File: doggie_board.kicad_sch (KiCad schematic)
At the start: 0 parts

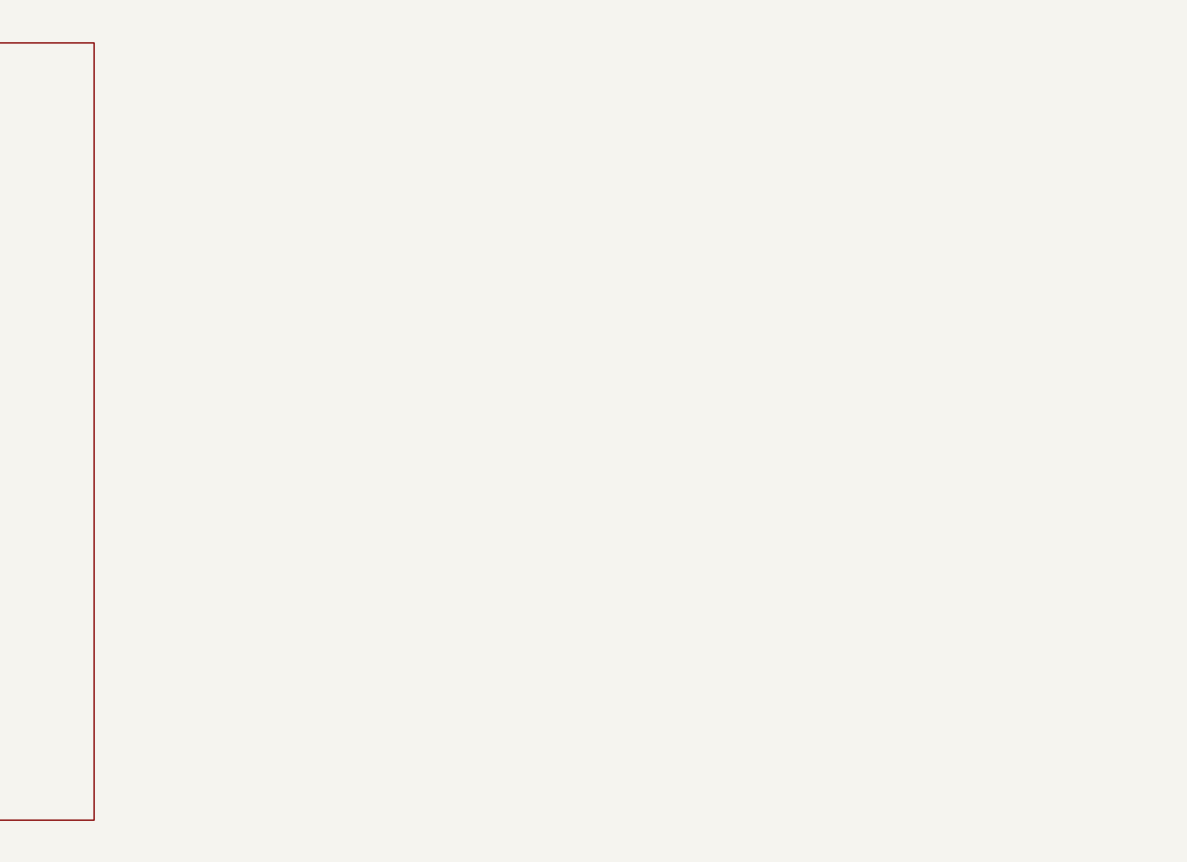
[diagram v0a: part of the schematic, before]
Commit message: Addition of Buck Converter
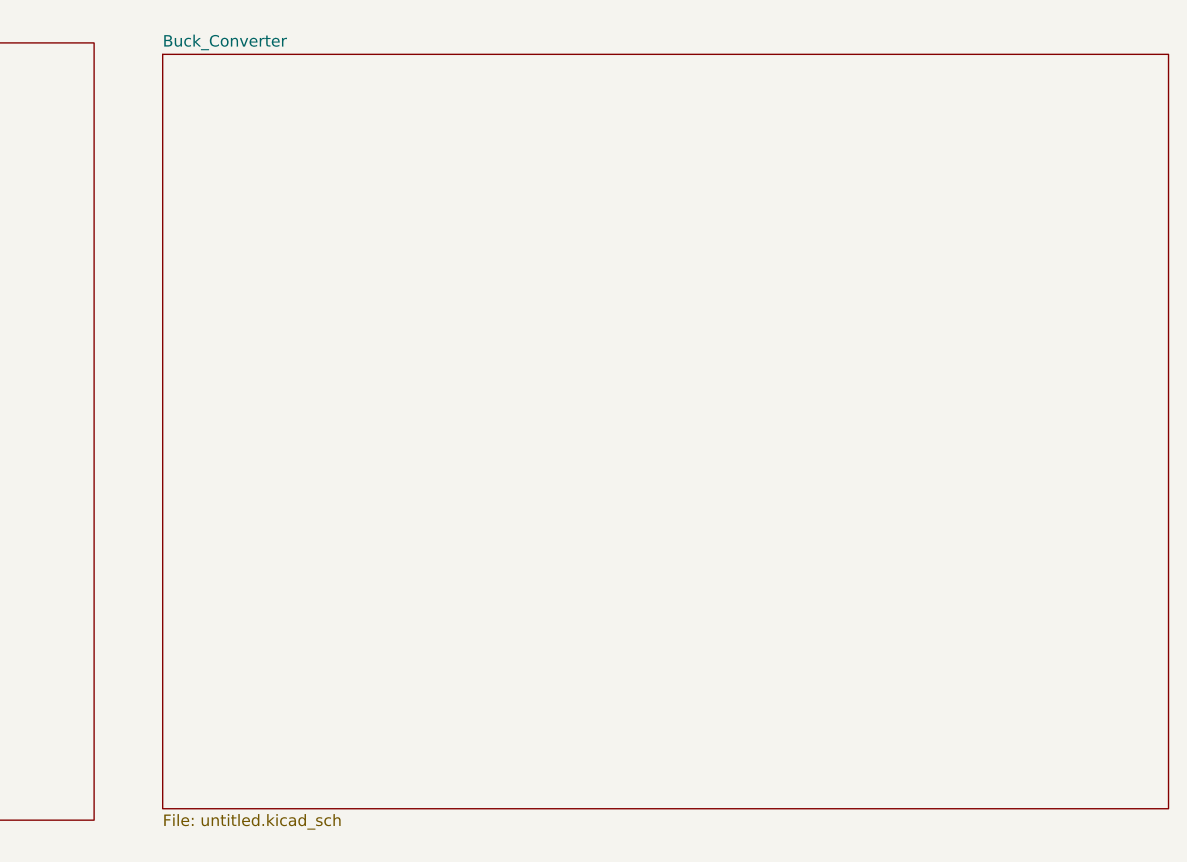
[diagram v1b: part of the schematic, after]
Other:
- added sheet Buck_Converter (untitled.kicad_sch)
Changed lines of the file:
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@@
+		)
+	)
+	(sheet
+		(at 157.48 19.05)
+		(size 111.76 83.82)
+		(exclude_from_sim no)
+		(in_bom yes)
+		(on_board yes)
+		(dnp no)
+		(fields_autoplaced yes)
+		(stroke
+			(width 0.1524)
+			(type solid)
+		)
+		(fill
+			(color 0 0 0 0.0000)
+		)
+		(property "Sheetname" "Buck_Converter"
+			(at 157.48 18.3384 0)
+			(effects
+				(font
+					(size 1.27 1.27)
+				)
+				(justify left bottom)
+			)
+		)
+		(property "Sheetfile" "untitled.kicad_sch"
+			(at 157.48 103.4546 0)
+			(effects
+				(font
+					(size 1.27 1.27)
+				)
+				(justify left top)
+			)
+		)
+		(instances
+			(project "doggie_board"
+				(path "/883cb7fa-3eb5-48d4-9cde-7c11307d94f0"
+					(page "3")
+				)
+			)
 		)
 	)

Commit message: Buck_Converter
Ensure it was properly pushed
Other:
- added sheet Buck_Converter_2 (buckconv2.kicad_sch)
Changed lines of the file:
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@@
 	(paper "A4")
+	(sheet
+		(at 15.24 115.57)
+		(size 41.91 16.51)
+		(exclude_from_sim no)
+		(in_bom yes)
+		(on_board yes)
+		(dnp no)
+		(fields_autoplaced yes)
+		(stroke
+			(width 0.1524)
+			(type solid)
+		)
+		(fill
+			(color 0 0 0 0.0000)
+		)
+		(property "Sheetname" "Buck_Converter_2"
+			(at 15.24 114.8584 0)
+			(effects
+				(font
+					(size 1.27 1.27)
+				)
+				(justify left bottom)
+			)
+		)
+		(property "Sheetfile" "buckconv2.kicad_sch"
+			(at 15.24 132.6646 0)
+			(effects
+				(font
+					(size 1.27 1.27)
+				)
+				(justify left top)
+			)
+		)
+		(instances
+			(project "doggie_board"
+				(path "/883cb7fa-3eb5-48d4-9cde-7c11307d94f0"
+					(page "4")
+				)
+			)
+		)
+	)
 	(sheet
 		(at 15.24 17.78)

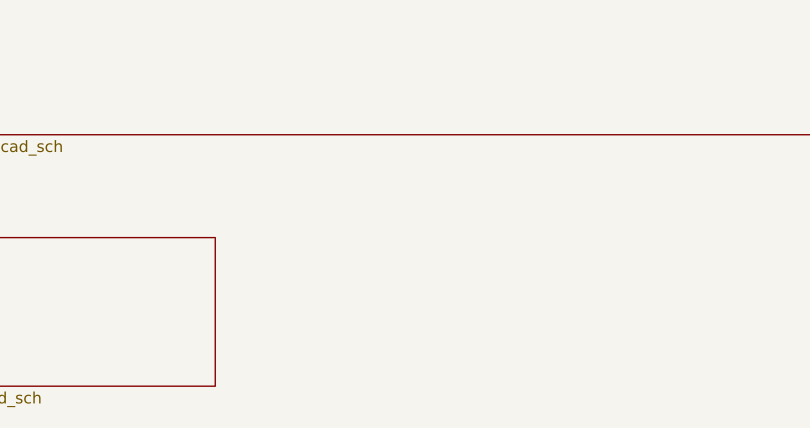
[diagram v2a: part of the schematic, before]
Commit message: fixed ERC errors and footprint for the TPS2490
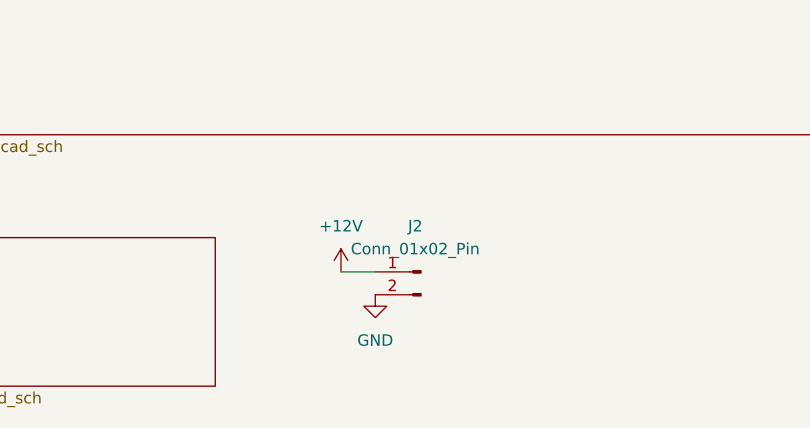
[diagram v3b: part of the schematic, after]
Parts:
- added J2: Conn_01x02_Pin, symbol Connector:Conn_01x02_Pin
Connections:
- new net +12V: J2.1 (Pin_1)
- new net GND: J2.2 (Pin_2)
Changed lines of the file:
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@@
 	(generator_version "9.0")
 	(paper "A4")
+	(wire
+		(pts
+			(xy 71.12 119.38) (xy 74.93 119.38)
+		)
+		(stroke
+			(width 0)
+			(type default)
+		)
+	)
+	(symbol
+		(lib_id "power:+12V")
+		(at 71.12 119.38 0)
+		(unit 1)
+		(exclude_from_sim no)
+		(in_bom yes)
+		(on_board yes)
+		(dnp no)
+		(fields_autoplaced yes)
+		(property "Reference" "#PWR015"
+			(at 71.12 123.19 0)
+			(effects
+				(font
+					(size 1.27 1.27)
+				)
+				(hide yes)
+			)
+		)
+		(property "Value" "+12V"
+			(at 71.12 114.3 0)
+			(effects
+				(font
+					(size 1.27 1.27)
+				)
+			)
+		)
+		(property "Footprint" ""
+			(at 71.12 119.38 0)
+			(effects
+				(font
+					(size 1.27 1.27)
+				)
+				(hide yes)
+			)
+		)
+		(property "Datasheet" ""
+			(at 71.12 119.38 0)
+			(effects
+				(font
+					(size 1.27 1.27)
+				)
+				(hide yes)
+			)
+		)
+		(property "Description" "Power symbol creates a global label with name \"+12V\""
+			(at 71.12 119.38 0)
+			(effects
+				(font
+					(size 1.27 1.27)
+				)
+				(hide yes)
+			)
+		)
+		(pin "1"
+		)
+		(instances
+			(project ""
+				(path "/883cb7fa-3eb5-48d4-9cde-7c11307d94f0"
+					(reference "#PWR015")
+					(unit 1)
+				)
+			)
+		)
+	)
+	(symbol
+		(lib_id "Connector:Conn_01x02_Pin")
+		(at 80.01 119.38 0)
+		(mirror y)
+		(unit 1)
+		(exclude_from_sim no)
+		(in_bom yes)
+		(on_board yes)
+		(dnp no)
+		(property "Reference" "J2"
+			(at 79.375 114.3 0)
+			(effects
+				(font
+					(size 1.27 1.27)
+				)
+			)
+		)
+		(property "Value" "Conn_01x02_Pin"
+			(at 79.375 116.84 0)
+			(effects
+				(font
+					(size 1.27 1.27)
+				)
+			)
+		)
+		(property "Footprint" ""
+			(at 80.01 119.38 0)
+			(effects
+				(font
+					(size 1.27 1.27)
+				)
+				(hide yes)
+			)
+		)
+		(property "Datasheet" "~"
+			(at 80.01 119.38 0)
+			(effects
+				(font
+					(size 1.27 1.27)
+				)
+				(hide yes)
+			)
+		)
+		(property "Description" "Generic connector, single row, 01x02, script generated"
+			(at 80.01 119.38 0)
+			(effects
+				(font
+					(size 1.27 1.27)
+				)
+				(hide yes)
+			)
+		)
+		(pin "1"
+		)
+		(pin "2"
+		)
+		(instances
+			(project ""
+				(path "/883cb7fa-3eb5-48d4-9cde-7c11307d94f0"
+					(reference "J2")
+					(unit 1)
+				)
+			)
+		)
+	)
+	(symbol
+		(lib_id "power:GND")
+		(at 74.93 121.92 0)
+		(unit 1)
+		(exclude_from_sim no)
+		(in_bom yes)
+		(on_board yes)
+		(dnp no)
+		(fields_autoplaced yes)
+		(property "Reference" "#PWR016"
+			(at 74.93 128.27 0)
+			(effects
+				(font
+					(size 1.27 1.27)
+				)
+				(hide yes)
+			)
+		)
+		(property "Value" "GND"
+			(at 74.93 127 0)
+			(effects
+				(font
+					(size 1.27 1.27)
+				)
+			)
+		)
+		(property "Footprint" ""
+			(at 74.93 121.92 0)
+			(effects
+				(font
+					(size 1.27 1.27)
+				)
+				(hide yes)
+			)
+		)
+		(property "Datasheet" ""
+			(at 74.93 121.92 0)
+			(effects
+				(font
+					(size 1.27 1.27)
+				)
+				(hide yes)
+			)
+		)
+		(property "Description" "Power symbol creates a global label with name \"GND\" , ground"
+			(at 74.93 121.92 0)
+			(effects
+				(font
+					(size 1.27 1.27)
+				)
+				(hide yes)
+			)
+		)
+		(pin "1"
+		)
+		(instances
+			(project ""
+				(path "/883cb7fa-3eb5-48d4-9cde-7c11307d94f0"
+					(reference "#PWR016")
+					(unit 1)
+				)
+			)
+		)
+	)
 	(sheet
 		(at 15.24 115.57)
